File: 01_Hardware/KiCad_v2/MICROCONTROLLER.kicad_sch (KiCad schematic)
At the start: 33 parts, among them Q500 NVTA7002NT1G, U500 DS3231M, U501 ESP32-WROOM-32E, U502 AT24CS01-SSHM

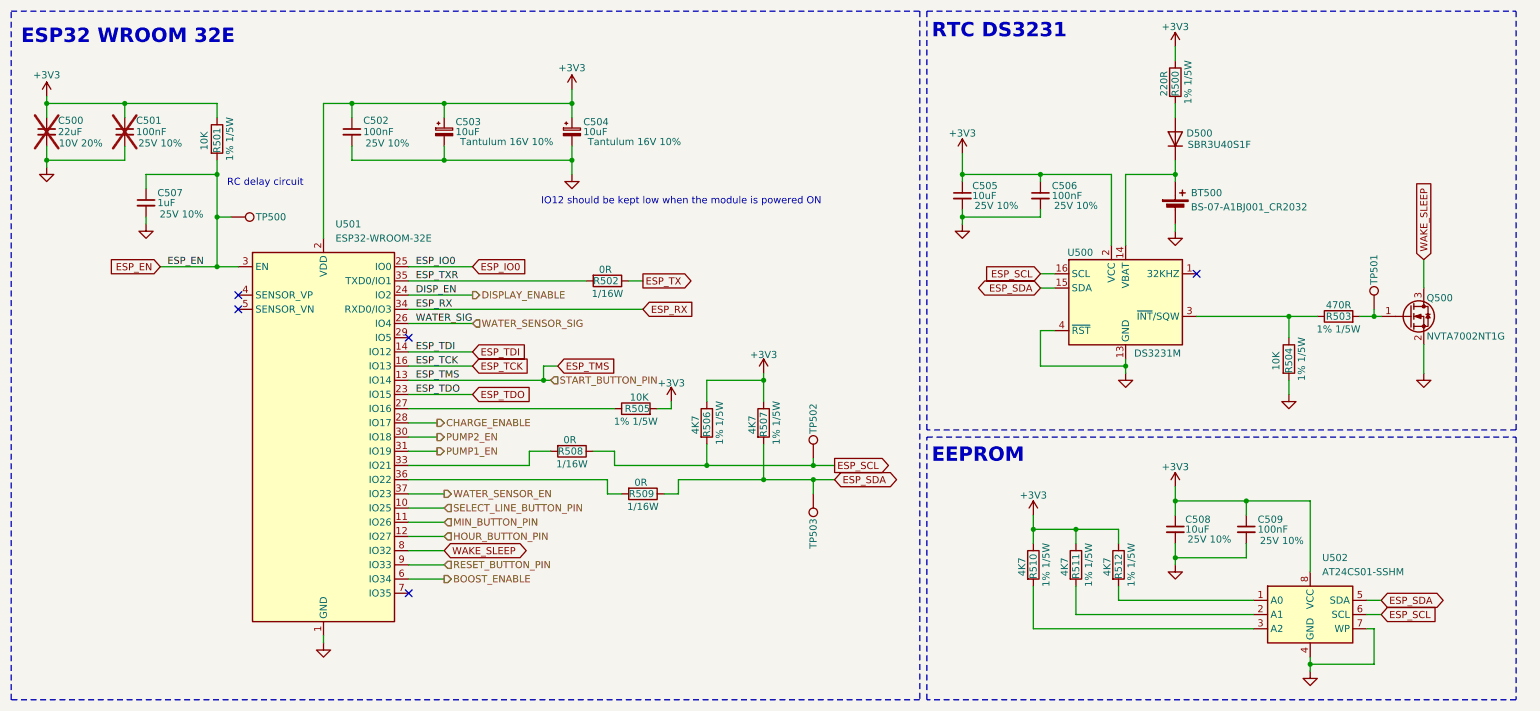
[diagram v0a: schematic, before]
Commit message: BOM done, except connectors/thermistor/button -> Will re-check BOM before sending to manufacturing
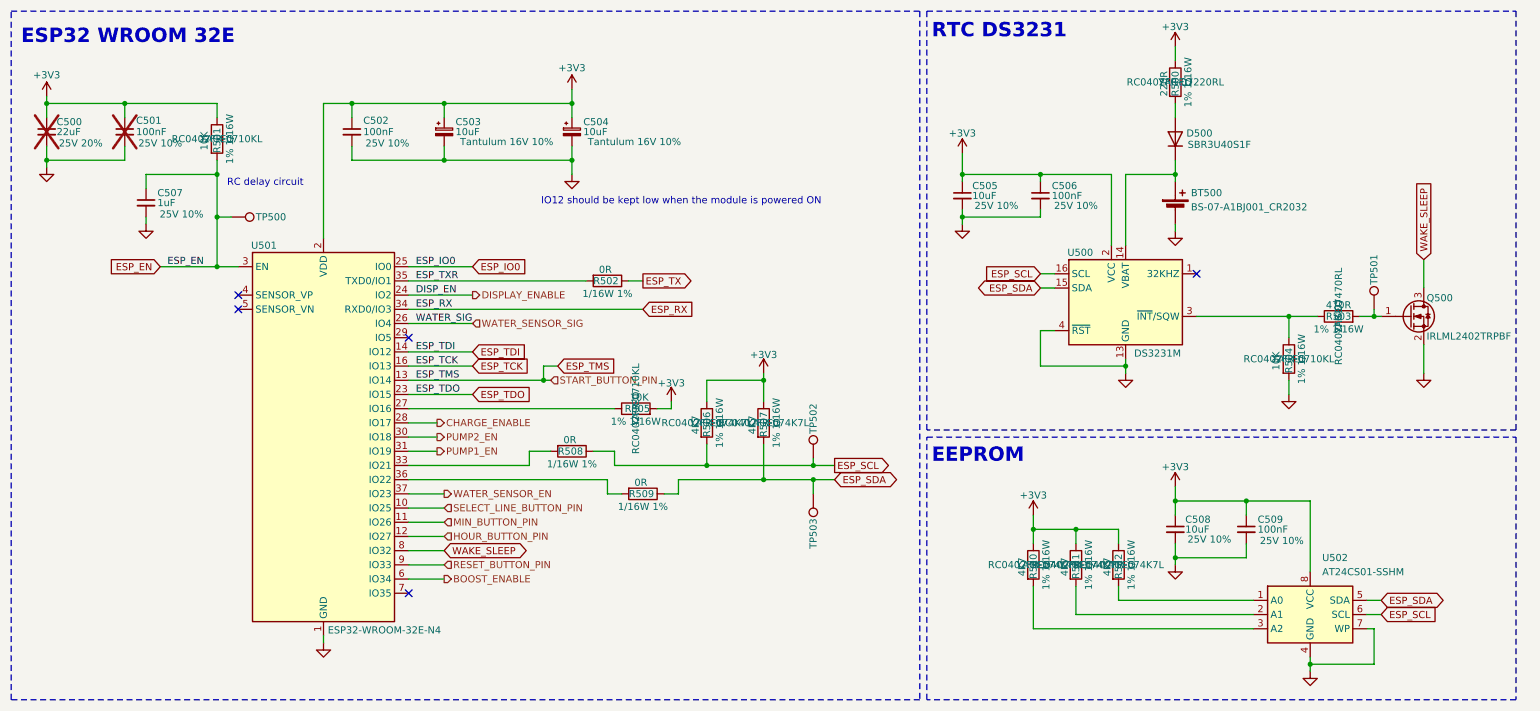
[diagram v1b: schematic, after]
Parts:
- C500: footprint Capacitor_SMD:C_0603_1608Metric -> Capacitor_SMD:C_0805_2012Metric; Link (none) -> https://jlcpcb.com/partdetail/46786-CL21A226MAQNNNE/C45783; Manufacturer (none) -> Samsung Electro-Mechanics; Manufacturer Part Number (none) -> CL21A226MAQNNNE
- C502, C506, C509: Manufacturer Samsung Electro-Mechanics -> Samsung Electro-Mechanics
- C505, C508: Manufacturer Murata Electronics -> Murata Electronics
- Q500: value NVTA7002NT1G -> IRLML2402TRPBF; footprint Custom_Global_Footprints:NVTA7002N -> Package_TO_SOT_SMD:SOT-23; Link (none) -> https://jlcpcb.com/partdetail/InfineonTechnologies-IRLML240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; Manufacturer (none) -> Infineon Technologies; Manufacturer Part Number (none) -> IRLML2402TRPBF
- R500: Manufacturer (none) -> YAGEO; Manufacturer Part Number (none) -> RC0402FR-07220RL
- R501, R504, R505: Manufacturer (none) -> YAGEO; Manufacturer Part Number (none) -> RC0402FR-0710KL
- R502, R508, R509: Manufacturer (none) -> YAGEO; Manufacturer Part Number (none) -> AC0402FR-070RL
- R503: Manufacturer (none) -> YAGEO; Manufacturer Part Number (none) -> RC0402FR-07470RL
- R506, R507, R510, R511, R512: Manufacturer (none) -> YAGEO; Manufacturer Part Number (none) -> RC0402FR-074K7L
- U501: value ESP32-WROOM-32E -> ESP32-WROOM-32E-N4; Manufacturer (none) -> Espressif Systems; Manufacturer Part Number (none) -> ESP32-WROOM-32E-N4

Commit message: USB-C and Serial PCB routing done
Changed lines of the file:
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@@
 					(size 1.27 1.27)
 				)
+				(hide yes)
 			)
 		)
@@
 					(size 1.27 1.27)
 				)
+				(hide yes)
 			)
 		)
@@
 					(size 1.27 1.27)
 				)
+				(hide yes)
 			)
 		)
@@
 					(size 1.27 1.27)
 				)
+				(hide yes)
 			)
 		)
@@
 					(size 1.27 1.27)
 				)
+				(hide yes)
 			)
 		)
@@
 					(size 1.27 1.27)
 				)
+				(hide yes)
 			)
 		)
@@
 					(size 1.27 1.27)
 				)
+				(hide yes)
 			)
 		)
@@
 					(size 1.27 1.27)
 				)
+				(hide yes)
 			)
 		)
@@
 					(size 1.27 1.27)
 				)
+				(hide yes)
 			)
 		)
@@
 					(size 1.27 1.27)
 				)
+				(hide yes)
 			)
 		)
@@
 					(size 1.27 1.27)
 				)
+				(hide yes)
 			)
 		)
@@
 					(size 1.27 1.27)
 				)
+				(hide yes)
 			)
 		)
@@
 					(size 1.27 1.27)
 				)
+				(hide yes)
 			)
 		)
@@
 					(size 1.27 1.27)
 				)
+				(hide yes)
 			)
 		)
@@
 					(size 1.27 1.27)
 				)
+				(hide yes)
 			)
 		)
@@
 					(size 1.27 1.27)
 				)
+				(hide yes)
 			)
 		)
@@
 					(size 1.27 1.27)
 				)
+				(hide yes)
 			)
 		)
@@
 					(size 1.27 1.27)
 				)
+				(hide yes)
 			)
 		)
@@
 					(size 1.27 1.27)
 				)
+				(hide yes)
 			)
 		)
@@
 					(size 1.27 1.27)
 				)
+				(hide yes)
 			)
 		)
@@
 					(size 1.27 1.27)
 				)
+				(hide yes)
 			)
 		)
@@
 					(size 1.27 1.27)
 				)
+				(hide yes)
 			)
 		)
@@
 					(size 1.27 1.27)
 				)
+				(hide yes)
 			)
 		)
@@
 					(size 1.27 1.27)
 				)
+				(hide yes)
 			)
 		)
@@
 					(size 1.27 1.27)
 				)
+				(hide yes)
 			)
 		)
@@
 					(size 1.27 1.27)
 				)
+				(hide yes)
 			)
 		)
@@
 					(size 1.27 1.27)
 				)
+				(hide yes)
 			)
 		)
@@
 					(size 1.27 1.27)
 				)
+				(hide yes)
 			)
 		)
@@
 					(size 1.27 1.27)
 				)
+				(hide yes)
 			)
 		)
@@
 					(size 1.27 1.27)
 				)
+				(hide yes)
 			)
 		)
@@
 					(size 1.27 1.27)
 				)
+				(hide yes)
 			)
 		)
@@
 					(size 1.27 1.27)
 				)
+				(hide yes)
 			)
 		)
@@
 					(size 1.27 1.27)
 				)
+				(hide yes)
 			)
 		)
@@
 					(size 1.27 1.27)
 				)
+				(hide yes)
 			)
 		)
@@
 					(size 1.27 1.27)
 				)
+				(hide yes)
 			)
 		)
@@
 					(size 1.27 1.27)
 				)
+				(hide yes)
 			)
 		)
@@
 					(size 1.27 1.27)
 				)
+				(hide yes)
 			)
 		)
@@
 					(size 1.27 1.27)
 				)
+				(hide yes)
 			)
 		)
@@
 					(size 1.27 1.27)
 				)
+				(hide yes)
 			)
 		)
@@
 					(size 1.27 1.27)
 				)
+				(hide yes)
 			)
 		)

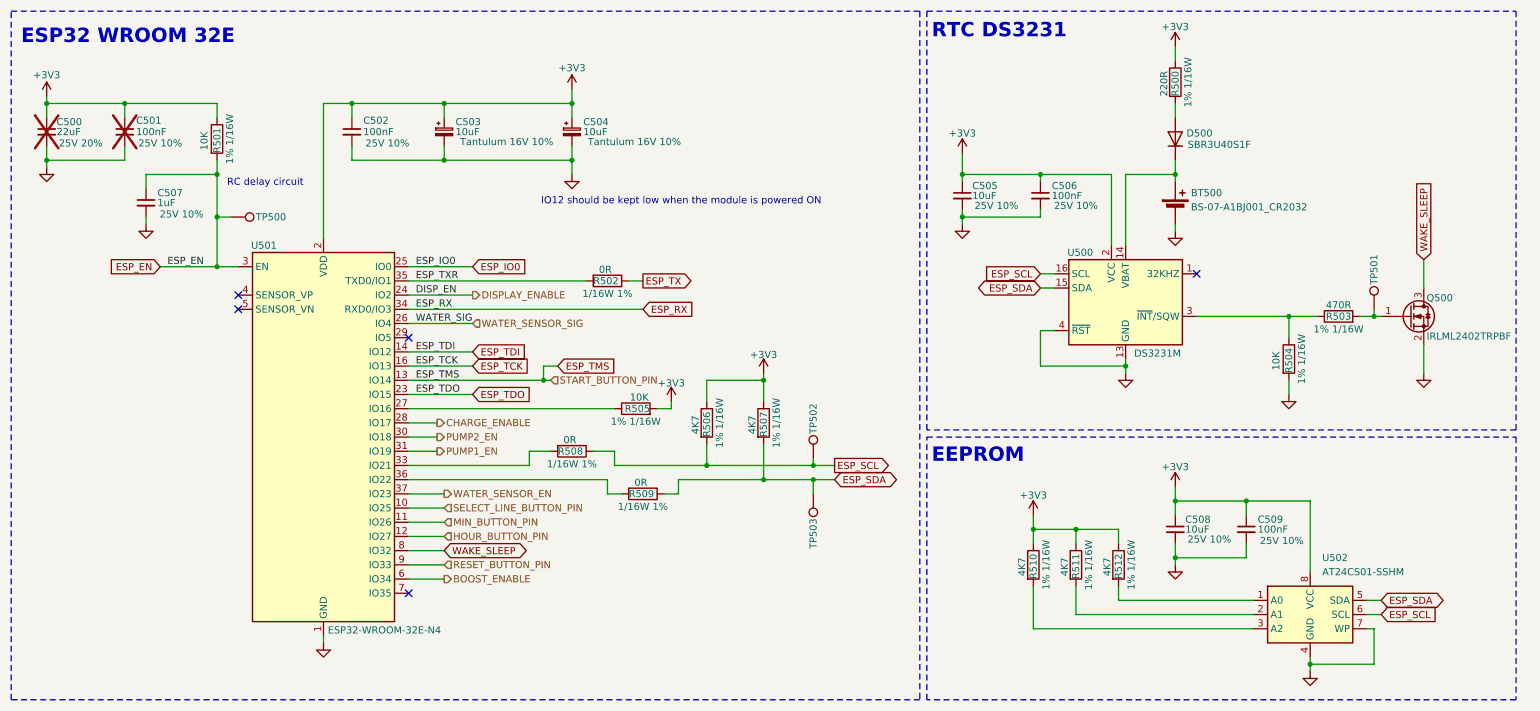
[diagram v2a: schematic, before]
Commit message: Power plane/rearranged connectors
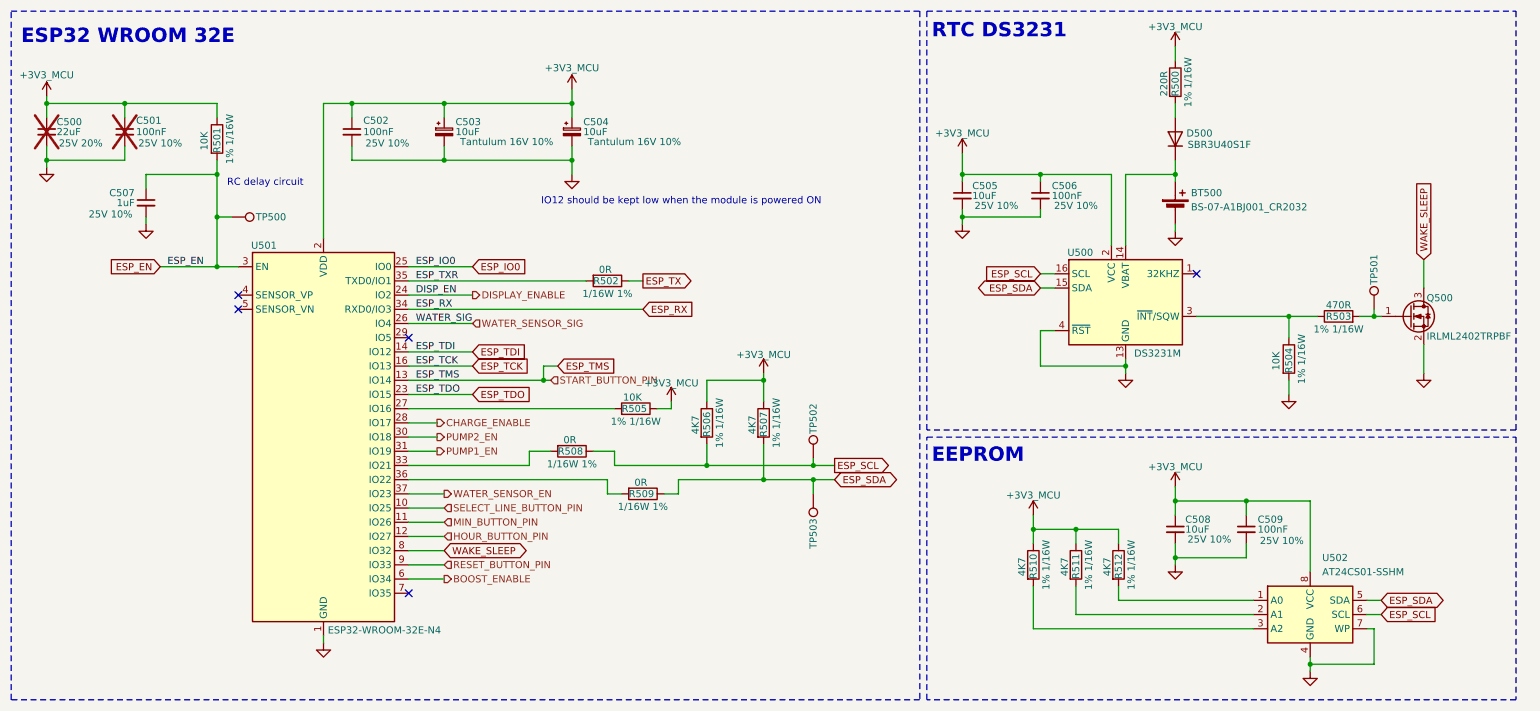
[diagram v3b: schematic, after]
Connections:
- net at U501.27 (IO16): now also R505.2; no longer R505.1
- net +3V3 renamed +3V3_MCU
- net +3V3_MCU: now also R505.1; no longer R505.2
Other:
- moved on the sheet: R505
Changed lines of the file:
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@@
 			)
 		)
-		(property "Value" "+3V3"
+		(property "Value" "+3V3_MCU"
 			(at 196.85 100.584 0)
 			(effects
@@
 			)
 		)
-		(property "Value" "+3V3"
+		(property "Value" "+3V3_MCU"
 			(at 132.08 80.518 0)
 			(effects
@@
 			)
 		)
-		(property "Value" "+3V3"
+		(property "Value" "+3V3_MCU"
 			(at 184.15 35.814 0)
 			(effects
@@
 			)
 		)
-		(property "Value" "+3V3"
+		(property "Value" "+3V3_MCU"
 			(at 148.59 75.438 0)
 			(effects
@@
 			)
 		)
-		(property "Value" "+3V3"
+		(property "Value" "+3V3_MCU"
 			(at 222.25 95.504 0)
 			(effects
@@
 			)
 		)
-		(property "Value" "+3V3"
+		(property "Value" "+3V3_MCU"
 			(at 114.3 24.13 0)
 			(effects
@@
 		(lib_id "Device:C_Small")
 		(at 38.1 48.26 0)
+		(mirror y)
 		(unit 1)
 		(exclude_from_sim no)
@@
 		(dnp no)
 		(property "Reference" "C507"
-			(at 40.132 46.482 0)
+			(at 36.068 46.482 0)
 			(effects
 				(font
@@
 		)
 		(property "Value" "1uF"
-			(at 40.132 48.26 0)
+			(at 36.068 48.26 0)
 			(effects
 				(font
@@
 		)
 		(property "Description" "25V 10%"
-			(at 44.45 50.292 0)
+			(at 31.75 50.292 0)
 			(effects
 				(font
@@
 		)
 		(property "Sim.Type" ""
-			(at 44.45 50.292 0)
+			(at 31.75 50.292 0)
 			(effects
 				(font
@@
 			)
 		)
-		(property "Value" "+3V3"
+		(property "Value" "+3V3_MCU"
 			(at 20.32 25.4 0)
 			(effects
@@
 			)
 		)
-		(property "Value" "+3V3"
+		(property "Value" "+3V3_MCU"
 			(at 222.25 16.764 0)
 			(effects
@@
 	(symbol
 		(lib_id "Device:R")
-		(at 125.73 85.09 90)
+		(at 125.73 85.09 270)
+		(mirror x)
 		(unit 1)
 		(exclude_from_sim no)
@@
 		(dnp no)
 		(property "Reference" "R505"
-			(at 128.27 85.09 90)
+			(at 123.19 85.09 90)
 			(effects
 				(font
@@
 		)
 		(property "Value" "10K"
-			(at 128.016 83.058 90)
+			(at 123.444 83.058 90)
 			(effects
 				(font

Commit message: Hardware for manufacturing v0.2
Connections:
- net BOOST_ENABLE: now also U501.24 (IO2); no longer U501.6 (IO34)
- net CHARGE_ENABLE: now also U501.10 (IO25); no longer U501.28 (IO17)
- net DISPLAY_ENABLE: now also U501.8 (IO32); no longer U501.24 (IO2)
- net HOUR_BUTTON_PIN: now also U501.29 (IO5); no longer U501.12 (IO27)
- net MIN_BUTTON_PIN: now also U501.28 (IO17); no longer U501.11 (IO26)
- net PUMP1_EN: now also U501.12 (IO27); no longer U501.31 (IO19)
- net PUMP2_EN: now also U501.11 (IO26); no longer U501.30 (IO18)
- net RESET_BUTTON_PIN: now also U501.30 (IO18); no longer U501.9 (IO33)
- net SELECT_LINE_BUTTON_PIN: now also U501.7 (IO35); no longer U501.10 (IO25)
- net WAKE_SLEEP: now also U501.26 (IO4); no longer U501.8 (IO32)
- net WATER_SENSOR_SIG: now also U501.31 (IO19); no longer U501.26 (IO4)
- new net START_BUTTON_PIN: U501.6 (IO34)
- no-connect marks 5 -> 4
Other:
- moved on the sheet: R508
